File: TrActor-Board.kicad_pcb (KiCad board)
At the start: 6 copper layers, 26 x 50 mm, 125 parts, among them J1 TagConnect, J2 Debug, J3 GCT4720, J4 Batt, J5 NTC, Q1 NMOS, SW1 Power, SW2 Reset, U1 nRF52833_QDxx, U2 DW3210, U3 ICM-40609, U4 ATX-13, U5 nPM1300, U6 USBLC6-2P6, U7 USBLC6-2P6, Y1 32MHz, Y2 32.768k

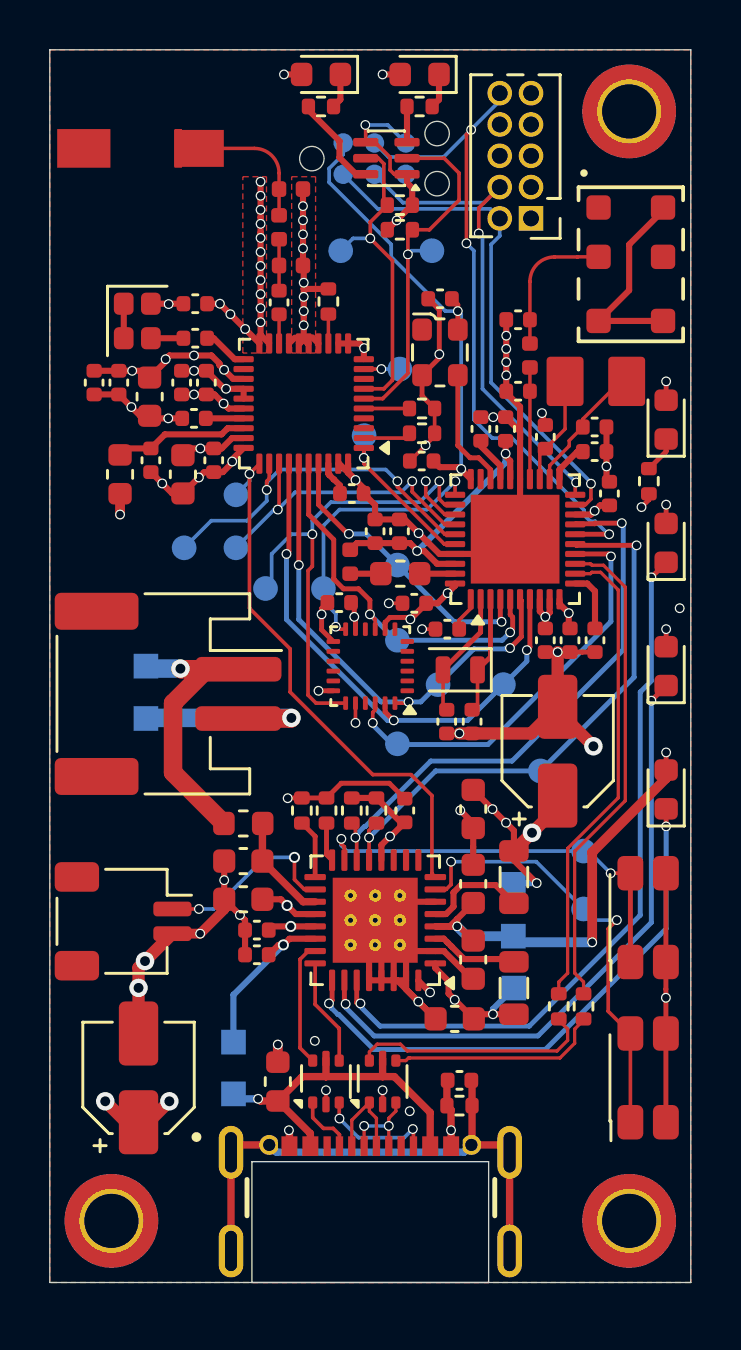
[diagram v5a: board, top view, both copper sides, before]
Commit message: minor fixes. ground pour on bottom layer and adding more 3d models. need to make a model for the NFC antenna
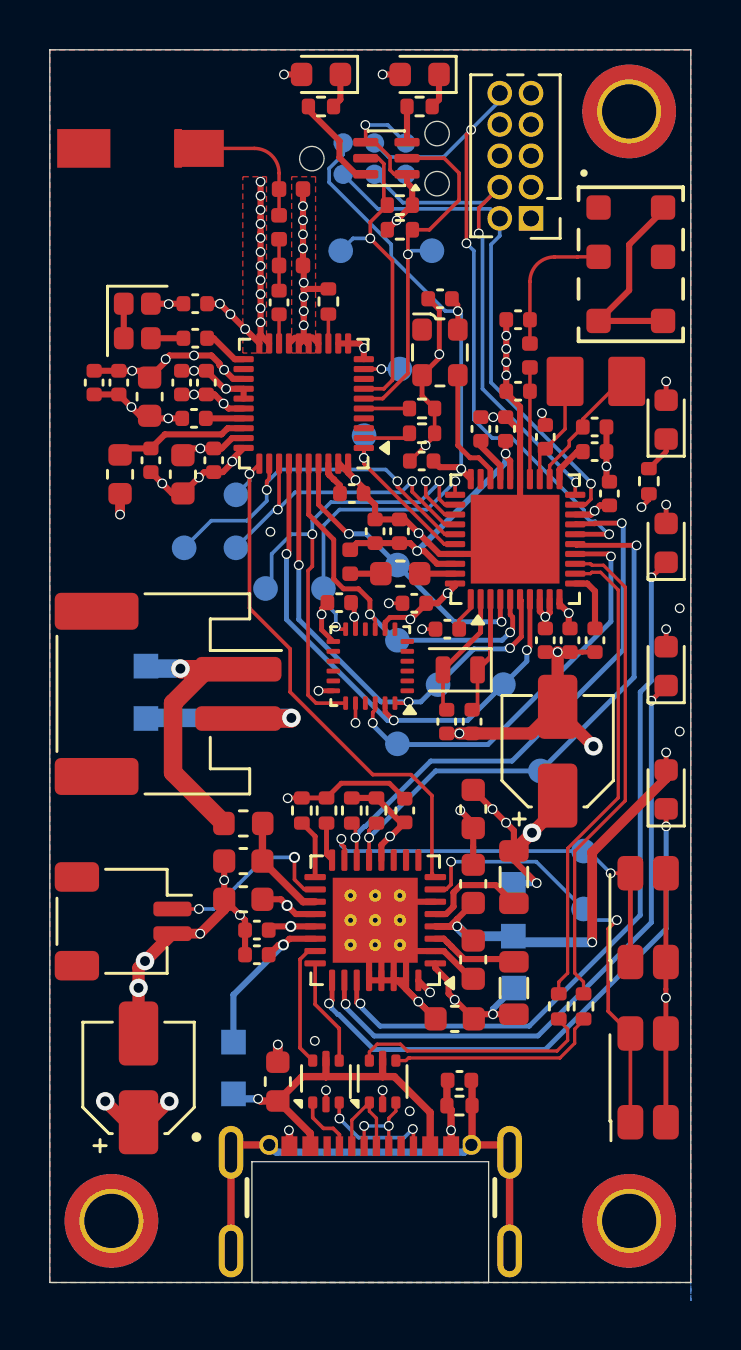
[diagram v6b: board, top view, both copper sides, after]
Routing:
- net GND: vias 68 -> 70
- added copper zone on B.Cu, net GND
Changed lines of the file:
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@@
 		(capping no)
 		(filling no)
-		(zone_defaults)
 		(pcbplotparams
 			(layerselection 0x00000000_00000000_00000000_020020ff)
@@
 		(sheetname "/")
 		(sheetfile "TrActor-Board.kicad_sch")
+		(units
+			(unit
+				(name "A")
+				(pins "SH" "B1" "B12" "A1" "A12" "A9" "B4" "B9" "A4" "A5" "B5" "A7" "B7"
+					"A6" "B6" "A8" "B8"
+				)
+			)
+		)
 		(attr smd)
 		(duplicate_pad_numbers_are_jumpers no)
@@
 		)
 		(embedded_fonts no)
+		(model "${KIPRJMOD}/TrActor.pretty/3dModel/SR4W035.step"
+			(offset
+				(xyz -2 3 0.25)
+			)
+			(scale
+				(xyz 1 1 1)
+			)
+			(rotate
+				(xyz -0 -0 90)
+			)
+		)
 	)
 	(footprint "Inductor_SMD:L_0402_1005Metric"
@@
 		)
 		(embedded_fonts no)
-		(model "${KICAD10_3DMODEL_DIR}/Oscillator.3dshapes/Oscillator_SMD_ECS_2520MV-xxx-xx-4Pin_2.5x2.0mm.step"
+		(model "${KIPRJMOD}/TrActor.pretty/3dModel/ECS-TXO-20CSMV-384-AY-TR.step"
 			(offset
 				(xyz 0 0 0)
@@
 			)
 			(rotate
-				(xyz 0 0 0)
+				(xyz -90 -0 -90)
 			)
 		)
@@
 		)
 		(embedded_fonts no)
-		(model "${KICAD10_3DMODEL_DIR}/Crystal.3dshapes/Crystal_SMD_2012-2Pin_2.0x1.2mm.step"
+		(model "${KIPRJMOD}/TrActor.pretty/3dModel/FC2012SN.stp"
 			(offset
 				(xyz 0 0 0)
@@
 			)
 			(rotate
-				(xyz 0 0 0)
+				(xyz -90 -0 -0)
 			)
 		)
@@
 		(sheetname "/MCU/")
 		(sheetfile "MCU.kicad_sch")
+		(units
+			(unit
+				(name "A")
+				(pins "24" "28" "29" "16" "20" "19" "1" "27" "38" "21" "26" "11" "8"
+					"30" "40" "18" "41" "37" "9" "25" "10" "39" "2" "3" "32" "31" "4" "5"
+					"22" "23" "7" "14" "15" "17" "33" "34" "35" "36" "6" "12" "13"
+				)
+			)
+		)
 		(attr smd)
 		(duplicate_pad_numbers_are_jumpers no)
@@
 			)
 		)
-		(attr smd dnp)
+		(attr smd)
 		(duplicate_pad_numbers_are_jumpers no)
 		(fp_line
@@
 		(sheetname "/Power Management/")
 		(sheetfile "power.kicad_sch")
+		(units
+			(unit
+				(name "A")
+				(pins "21" "23" "24" "19" "18" "7" "8" "9" "10" "11" "25" "26" "27" "17"
+					"16" "15" "14" "13" "12" "33" "22" "20" "4" "1" "3" "2" "32" "5" "6"
+					"28" "30" "29" "31"
+				)
+			)
+		)
 		(attr smd)
 		(duplicate_pad_numbers_are_jumpers no)
@@
 	)
 	(via
+		(at 162.55 97.65)
+		(size 0.4)
+		(drill 0.3)
+		(layers "F.Cu" "B.Cu")
+		(free yes)
+		(net "GND")
+	)
+	(via
 		(at 145.55 77.06)
 		(size 0.4)
@@
 	)
 	(via
+		(at 145.95 89.55)
+		(size 0.4)
+		(drill 0.3)
+		(layers "F.Cu" "B.Cu")
+		(free yes)
+		(net "GND")
+	)
+	(via
 		(at 161.99 108.45)
 		(size 0.4)
@@
 			)
 		)
+	)
+	(zone
+		(net "GND")
+		(layer "B.Cu")
+		(name "Back Ground Pour")
+		(hatch edge 0.5)
+		(priority 5)
+		(connect_pads yes
+			(clearance 0.3)
+		)
+		(min_thickness 0.2)
+		(fill yes
+			(thermal_gap 0.5)
+			(thermal_bridge_width 0.5)
+			(island_removal_mode 0)
+		)
+		(polygon
+			(pts
+				(xy 137 70) (xy 163 70) (xy 163 120.75) (xy 163 120) (xy 137 120)
+			)
+		)
